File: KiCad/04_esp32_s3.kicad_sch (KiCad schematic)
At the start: 1 part, among them IC101 ESP32-S3-WROOM-1-N16R8

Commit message: Update power scheme
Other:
- note added: "[4] ESP32 S3"
- moved on the sheet: IC101
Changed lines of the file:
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@@
 	(generator_version "9.0")
 	(paper "A4")
+	(text "[4] ESP32 S3"
+		(exclude_from_sim no)
+		(at 43.18 21.336 0)
+		(effects
+			(font
+				(size 5.08 5.08)
+			)
+		)
+	)
 	(wire
 		(pts
-			(xy 95.25 73.66) (xy 101.6 73.66)
+			(xy 165.1 72.39) (xy 171.45 72.39)
 		)
 		(stroke
@@
 	(wire
 		(pts
-			(xy 95.25 76.2) (xy 101.6 76.2)
+			(xy 165.1 74.93) (xy 171.45 74.93)
 		)
 		(stroke
@@
 	(global_label "USB_D+"
 		(shape input)
-		(at 101.6 76.2 0)
+		(at 171.45 74.93 0)
 		(fields_autoplaced yes)
 		(effects
@@
 		)
 		(property "Intersheetrefs" "${INTERSHEET_REFS}"
-			(at 112.2052 76.2 0)
+			(at 182.0552 74.93 0)
 			(effects
 				(font
@@
 	(global_label "USB_D-"
 		(shape input)
-		(at 101.6 73.66 0)
+		(at 171.45 72.39 0)
 		(fields_autoplaced yes)
 		(effects
@@
 		)
 		(property "Intersheetrefs" "${INTERSHEET_REFS}"
-			(at 112.2052 73.66 0)
+			(at 182.0552 72.39 0)
 			(effects
 				(font
@@
 	(symbol
 		(lib_id "esp32_s3_weather_webserver:ESP32-S3-WROOM-1-N16R8")
-		(at 62.23 55.88 0)
+		(at 132.08 54.61 0)
 		(unit 1)
 		(exclude_from_sim no)
@@
 		(dnp no)
 		(property "Reference" "IC101"
-			(at 80.518 53.086 0)
+			(at 150.368 51.816 0)
 			(effects
 				(font
@@
 		)
 		(property "Value" "ESP32-S3-WROOM-1-N16R8"
-			(at 91.948 54.864 0)
+			(at 161.798 53.594 0)
 			(effects
 				(font
@@
 		)
 		(property "Footprint" "esp32_s3_weather_webserver:ESP32S3WROOM1N16R8"
-			(at 91.44 150.8 0)
+			(at 161.29 149.53 0)
 			(effects
 				(font
@@
 		)
 		(property "Datasheet" "https://www.espressif.com/sites/default/files/documentation/esp32-s3-wroom-1_wroom-1u_datasheet_en.pdf"
-			(at 91.44 250.8 0)
+			(at 161.29 249.53 0)
 			(effects
 				(font
@@
 		)
 		(property "Description" "Multiprotocol Modules SMD Module, ESP32-S3R8, 3.3V, 8 MB Octal PSRAM Die, 16 MB Quad SPI Flash, PCB Antenna"
-			(at 73.406 167.64 0)
+			(at 143.256 166.37 0)
 			(effects
 				(font
@@
 		)
 		(property "Height" "3.25"
-			(at 91.44 450.8 0)
+			(at 161.29 449.53 0)
 			(effects
 				(font
@@
 		)
 		(property "Manufacturer_Name" "Espressif Systems"
-			(at 91.44 550.8 0)
+			(at 161.29 549.53 0)
 			(effects
 				(font
@@
 		)
 		(property "Manufacturer_Part_Number" "ESP32-S3-WROOM-1-N16R8"
-			(at 91.44 650.8 0)
+			(at 161.29 649.53 0)
 			(effects
 				(font
@@
 		)
 		(property "Mouser Part Number" "356-ESP32S3WRM1N16R8"
-			(at 91.44 750.8 0)
+			(at 161.29 749.53 0)
 			(effects
 				(font
@@
 		)
 		(property "Mouser Price/Stock" "https://www.mouser.co.uk/ProductDetail/Espressif-Systems/ESP32-S3-WROOM-1-N16R8?qs=Li%252BoUPsLEnvQc9gW6AMhZg%3D%3D"
-			(at 91.44 850.8 0)
+			(at 161.29 849.53 0)
 			(effects
 				(font
@@
 		)
 		(property "Arrow Part Number" ""
-			(at 91.44 950.8 0)
+			(at 161.29 949.53 0)
 			(effects
 				(font
@@
 		)
 		(property "Arrow Price/Stock" ""
-			(at 91.44 1050.8 0)
+			(at 161.29 1049.53 0)
 			(effects
 				(font

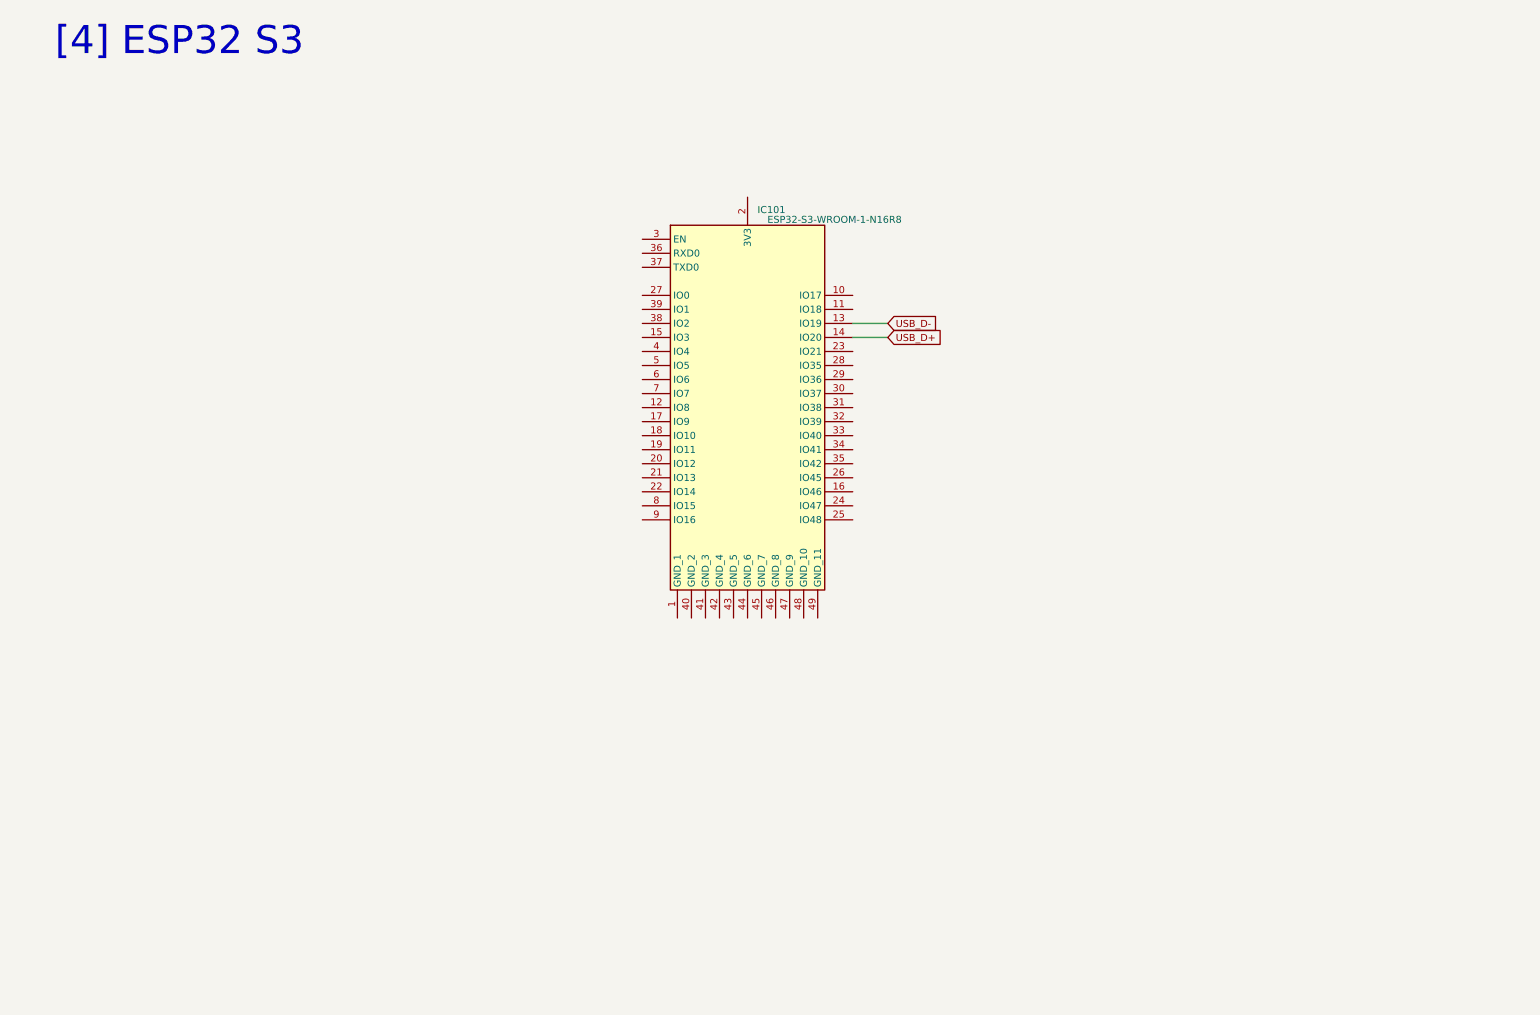
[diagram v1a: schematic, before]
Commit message: Update ESP32 Scheme
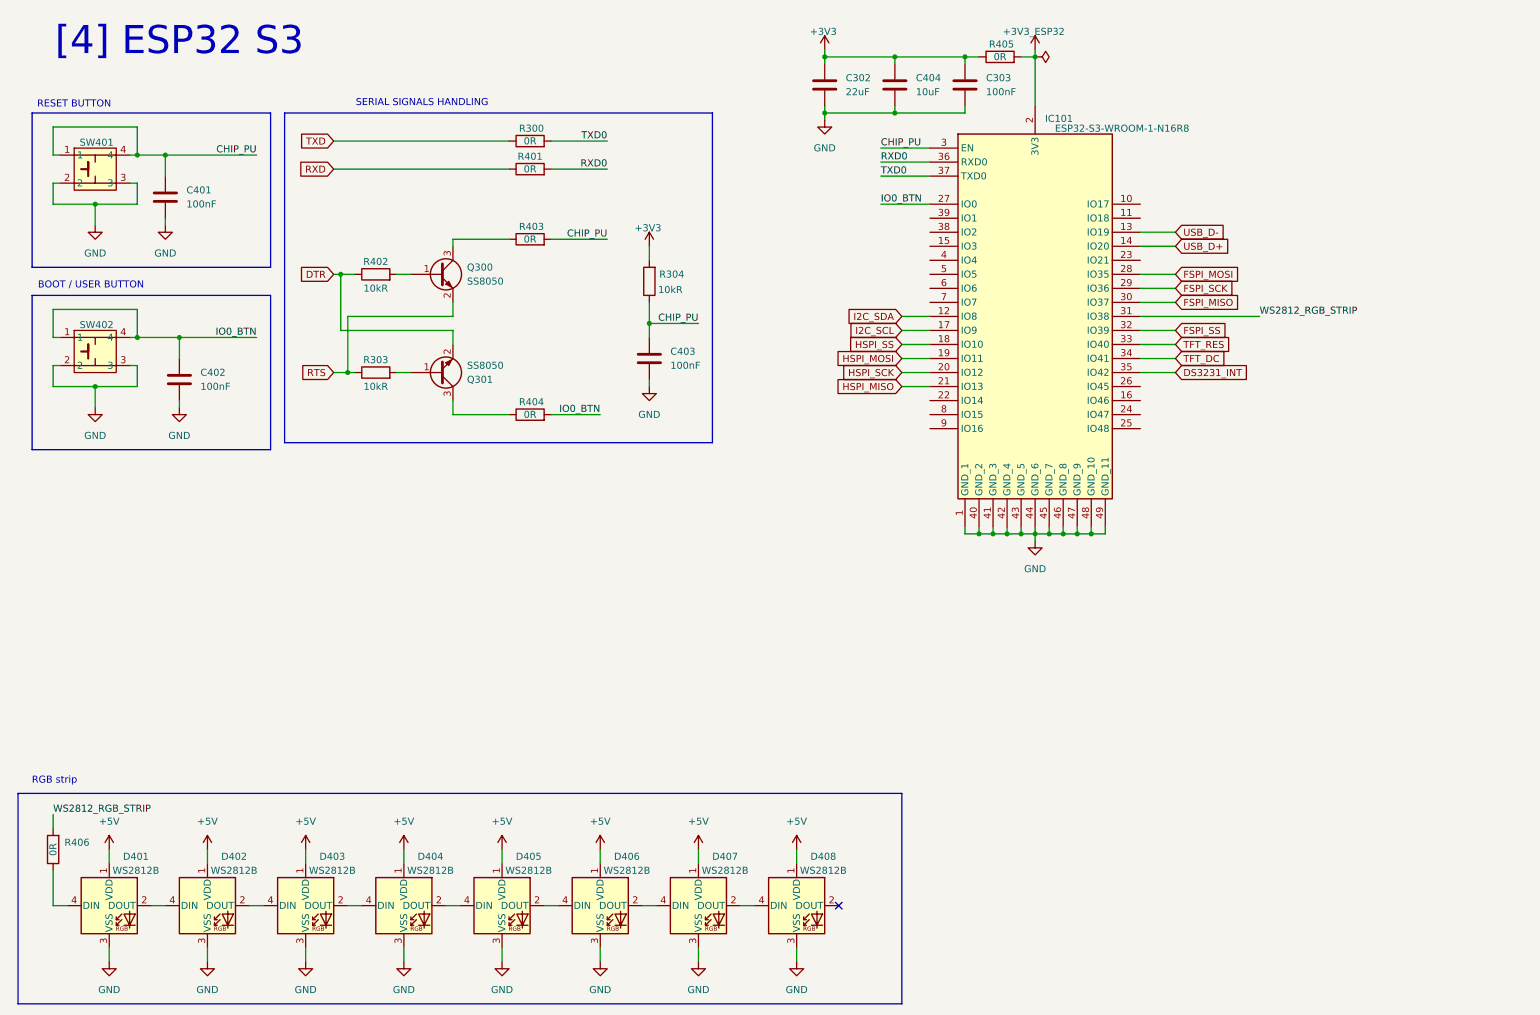
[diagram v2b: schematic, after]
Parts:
- added C302: 22uF, Capacitor_SMD:C_0603_1608Metric, symbol Device:C
- added C303, C401, C402, C403: 100nF, Capacitor_SMD:C_0603_1608Metric, symbol Device:C
- added C404: 10uF, Capacitor_SMD:C_0603_1608Metric, symbol Device:C
- added D401, D402, D403, D404, D405, D406, D407, D408: WS2812B, LED_SMD:LED_WS2812B_PLCC4_5.0x5.0mm_P3.2mm, symbol LED:WS2812B
- added Q300, Q301: SS8050, Package_TO_SOT_SMD:SOT-23, symbol Transistor_BJT:SS8050
- added R300, R401, R403, R404, R405, R406: 0R, Resistor_SMD:R_0805_2012Metric, symbol Device:R
- added R303, R304, R402: 10kR, Resistor_SMD:R_0805_2012Metric, symbol Device:R
- added SW401, SW402: ~, esp32_s3_weather_webserver:SW_PUSH_6mm_H5mm, symbol esp32_s3_weather_webserver:SW_PUSH_6mm_H5mm
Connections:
- net GND: now reaches IC101.1 (GND_1)
- net GND: now also IC101.40 (GND_2), IC101.41 (GND_3), IC101.42 (GND_4), IC101.43 (GND_5), IC101.44 (GND_6), IC101.45 (GND_7), IC101.46 (GND_8), IC101.47 (GND_9), IC101.48 (GND_10), IC101.49 (GND_11), C302.2, C303.2, C401.2, C402.2, C403.2, C404.2, D401.3 (VSS), D402.3 (VSS), D403.3 (VSS), D404.3 (VSS), D405.3 (VSS), D406.3 (VSS), D407.3 (VSS), D408.3 (VSS), SW401.2, SW401.3, SW402.2, SW402.3
- net I2C_SDA: now reaches IC101.12 (IO8)
- net I2C_SCL: now reaches IC101.17 (IO9)
- net HSPI_SS: now reaches IC101.18 (IO10)
- net HSPI_MOSI: now reaches IC101.19 (IO11)
- net +3V3_ESP32: now reaches IC101.2 (3V3)
- net +3V3_ESP32: now also R405.2
- net HSPI_SCK: now reaches IC101.20 (IO12)
- net HSPI_MISO: now reaches IC101.21 (IO13)
- net IO0_BTN: now reaches IC101.27 (IO0)
- net IO0_BTN: now also C402.1, R404.2, SW402.1, SW402.4
- net FSPI_MOSI: now reaches IC101.28 (IO35)
- net FSPI_SCK: now reaches IC101.29 (IO36)
- net CHIP_PU: now reaches IC101.3 (EN)
- net CHIP_PU: now also C401.1, C403.1, R304.1, R403.2, SW401.1, SW401.4
- net FSPI_MISO: now reaches IC101.30 (IO37)
- net WS2812_RGB_STRIP: now reaches IC101.31 (IO38)
- net WS2812_RGB_STRIP: now also R406.2
- net FSPI_SS: now reaches IC101.32 (IO39)
- net TFT_RES: now reaches IC101.33 (IO40)
- net TFT_DC: now reaches IC101.34 (IO41)
- net DS3231_INT: now reaches IC101.35 (IO42)
- net RXD0: now reaches IC101.36 (RXD0)
- net RXD0: now also R401.2
- net TXD0: now reaches IC101.37 (TXD0)
- net TXD0: now also R300.2
- new net: D407.2 (DOUT), D408.4 (DIN)
- new net: Q300.1 (B), R402.2
- new net: Q300.3 (C), R403.1
- new net: D401.2 (DOUT), D402.4 (DIN)
- new net: D401.4 (DIN), R406.1
- new net: D403.2 (DOUT), D404.4 (DIN)
- new net: D402.2 (DOUT), D403.4 (DIN)
- new net: D406.2 (DOUT), D407.4 (DIN)
- new net: Q301.3 (C), R404.1
- new net: Q301.1 (B), R303.2
- new net: D405.2 (DOUT), D406.4 (DIN)
- new net: D404.2 (DOUT), D405.4 (DIN)
- new net +3V3: C302.1, C303.1, C404.1, R304.2, R405.1
- new net +5V: D401.1 (VDD), D402.1 (VDD), D403.1 (VDD), D404.1 (VDD), D405.1 (VDD), D406.1 (VDD), D407.1 (VDD), D408.1 (VDD)
- new net DTR: Q301.2 (E), R402.1
- new net RTS: Q300.2 (E), R303.1
- new net RXD: R401.1
- new net TXD: R300.1
- no-connect marks 0 -> 1
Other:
- note added: "BOOT / USER BUTTON"
- note added: "RESET BUTTON"
- note added: "RGB strip"
- note added: "SERIAL SIGNALS HANDLING"
- moved on the sheet: IC101

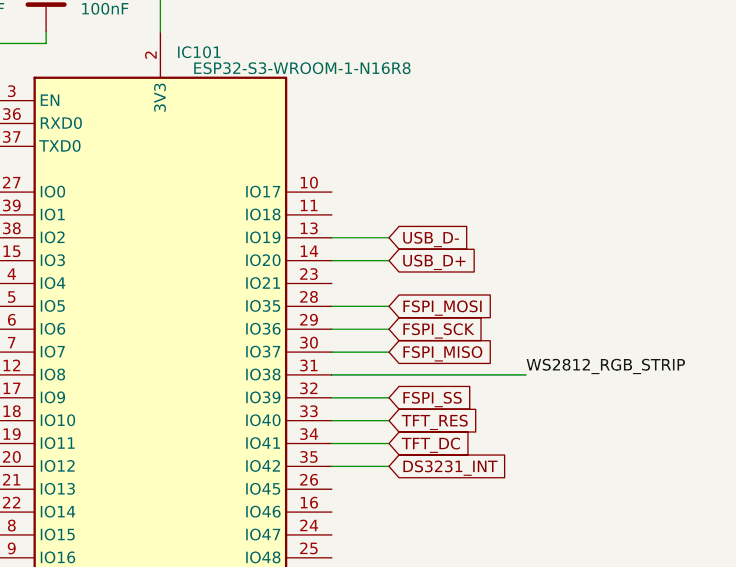
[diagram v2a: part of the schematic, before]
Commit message: Add SD card to scheme
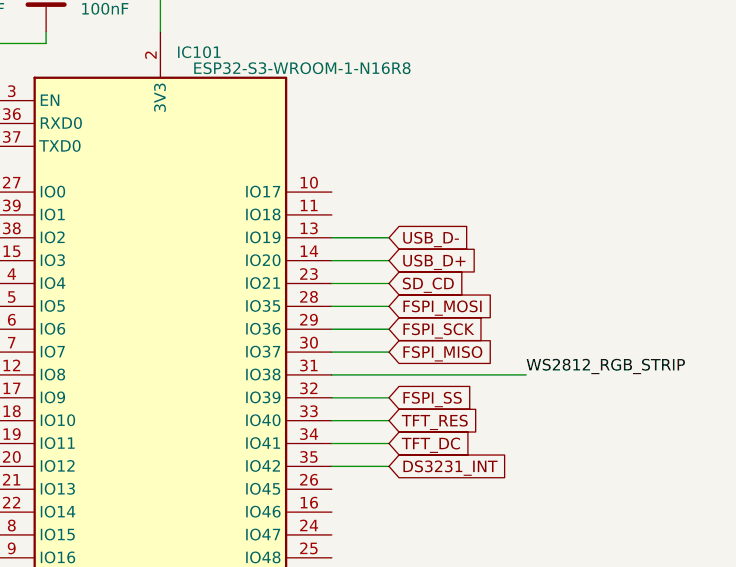
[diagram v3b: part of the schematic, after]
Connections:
- net SD_CD: now reaches IC101.23 (IO21)
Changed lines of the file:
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@@
+	(wire
+		(pts
+			(xy 217.17 60.96) (xy 223.52 60.96)
+		)
+		(stroke
+			(width 0)
+			(type default)
+		)
+	)
 	(wire
 		(pts
@@
 				(hide yes)
 			)
+		)
+	)
+	(global_label "SD_CD"
+		(shape input)
+		(at 223.52 60.96 0)
+		(fields_autoplaced yes)
+		(effects
+			(font
+				(size 1.27 1.27)
+			)
+			(justify left)
+		)
+		(property "Intersheetrefs" "${INTERSHEET_REFS}"
+			(at 232.4923 60.96 0)
+			(effects
+				(font
+					(size 1.27 1.27)
+				)
+				(justify left)
+				(hide yes)
+			)

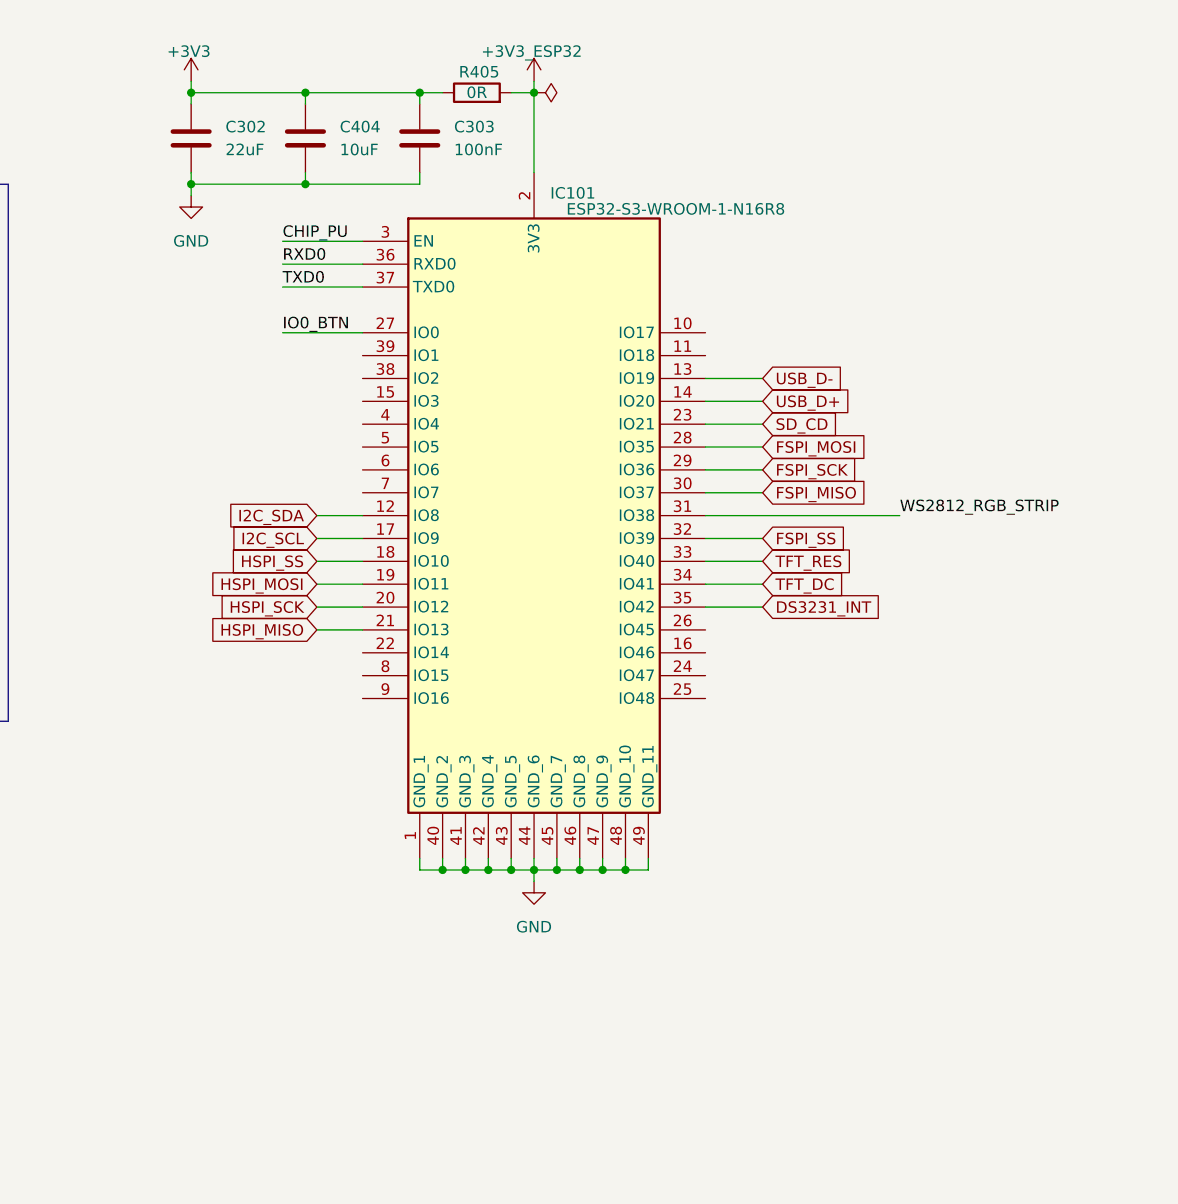
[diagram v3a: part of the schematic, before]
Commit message: Add DS3231
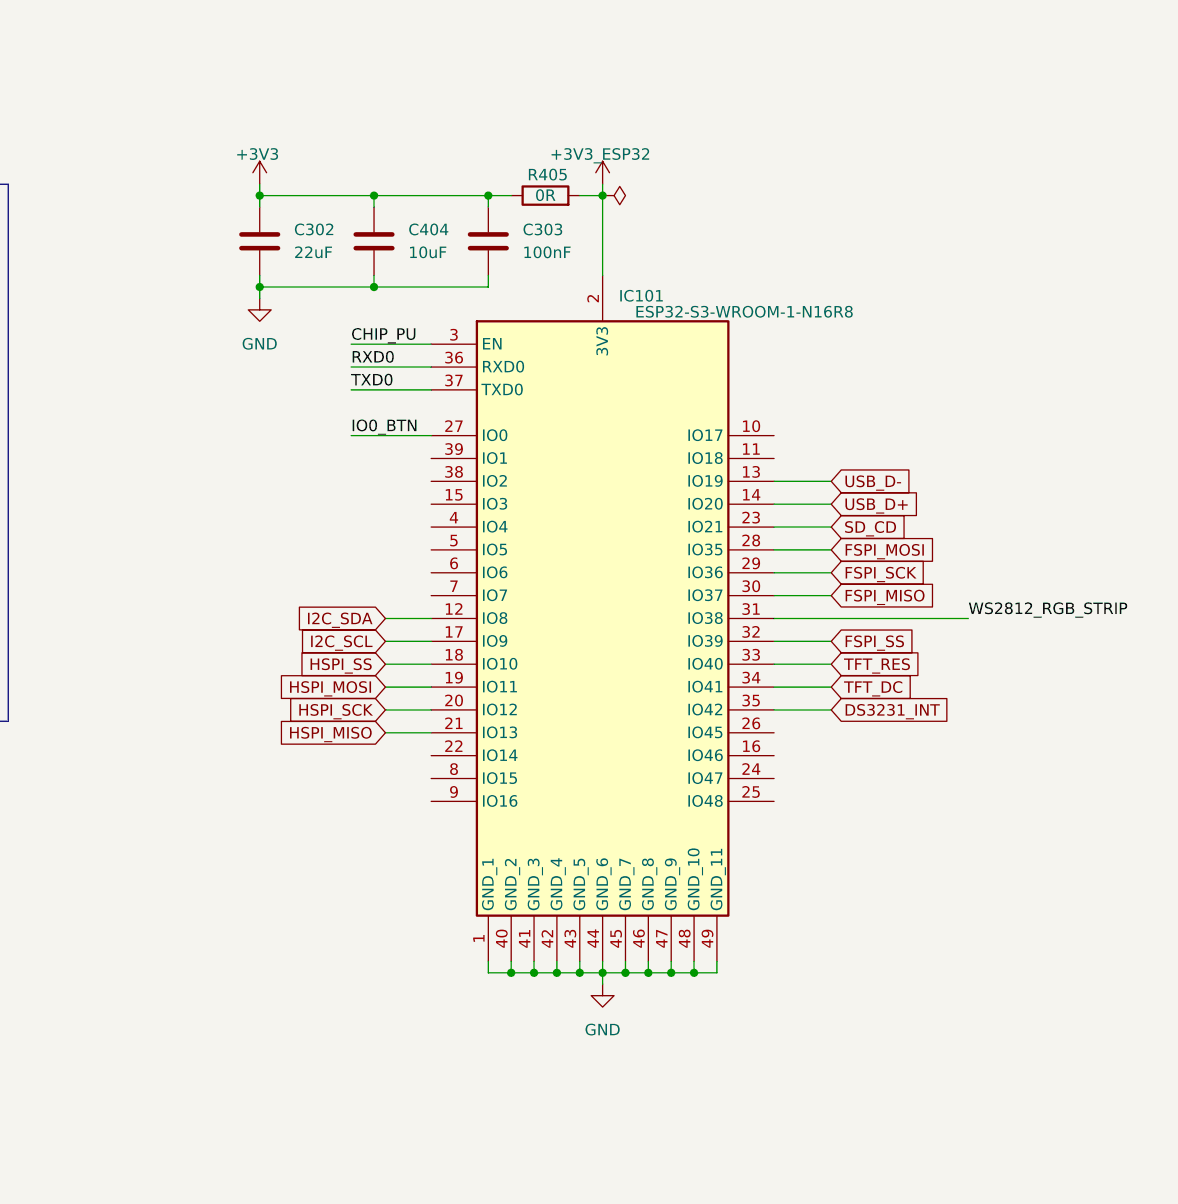
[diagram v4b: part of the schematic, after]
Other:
- moved on the sheet: C302, C303, C404, IC101, R405
